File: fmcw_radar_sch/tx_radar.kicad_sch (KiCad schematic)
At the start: 16 parts, among them SW2 SW_Nidec_CAS-120A1, U4 ADAR2001ACCZ

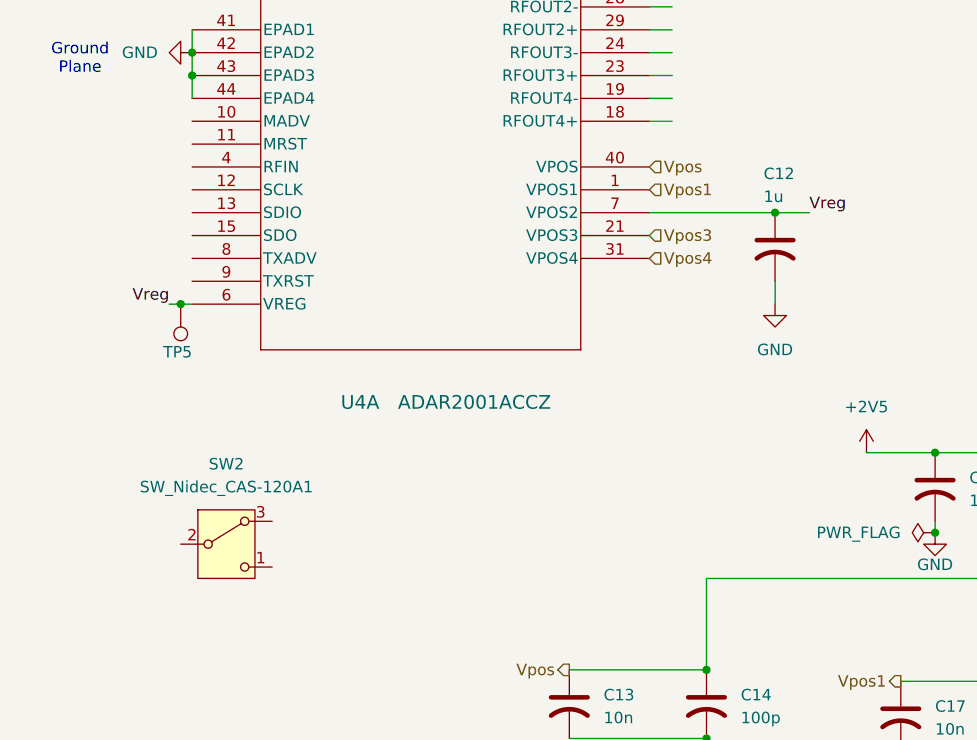
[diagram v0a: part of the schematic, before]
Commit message: Layout of controller board
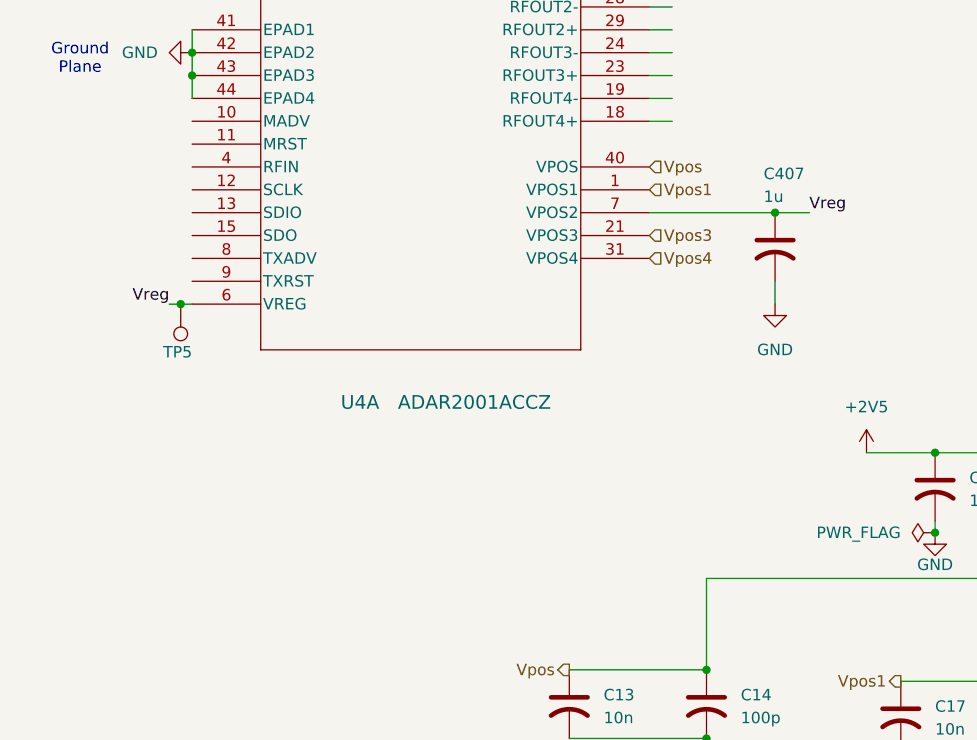
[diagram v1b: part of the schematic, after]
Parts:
- removed C12: 1u, symbol Device:C_US
- removed SW2: SW_Nidec_CAS-120A1, Button_Switch_SMD:Nidec_Copal_CAS-120A, symbol Switch:SW_Nidec_CAS-120A1
- added C407: 1u, symbol Device:C_US
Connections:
- net GND: now also C407.2
- net Vreg: now also C407.1
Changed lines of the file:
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@@
+	)
+	(junction
+		(at 101.6 82.55)
+		(diameter 0)
+		(color 0 0 0 0)
 	)
 	(junction
@@
 	)
 	(junction
-		(at 101.6 82.55)
-		(diameter 0)
-		(color 0 0 0 0)
-	)
-	(junction
 		(at 138.43 123.19)
 		(diameter 0)
@@
 	(wire
 		(pts
+			(xy 101.6 82.55) (xy 105.41 82.55)
+		)
+		(stroke
+			(width 0)
+			(type default)
+		)
+	)
+	(wire
+		(pts
 			(xy 87.63 57.15) (xy 90.17 57.15)
 		)
@@
 	(wire
 		(pts
-			(xy 101.6 82.55) (xy 105.41 82.55)
+			(xy 87.63 82.55) (xy 101.6 82.55)
 		)
 		(stroke
@@
 		(pts
 			(xy 199.39 123.19) (xy 199.39 134.62)
-		)
-		(stroke
-			(width 0)
-			(type default)
-		)
-	)
-	(wire
-		(pts
-			(xy 87.63 82.55) (xy 101.6 82.55)
 		)
 		(stroke
@@
 	)
 	(symbol
-		(lib_id "Switch:SW_Nidec_CAS-120A1")
-		(at 40.64 119.38 0)
-		(unit 1)
-		(exclude_from_sim no)
-		(in_bom yes)
-		(on_board yes)
-		(dnp no)
-		(fields_autoplaced yes)
-		(property "Reference" "SW2"
-			(at 40.64 110.49 0)
-			(effects
-				(font
-					(size 1.27 1.27)
-				)
-			)
-		)
-		(property "Value" "SW_Nidec_CAS-120A1"
-			(at 40.64 113.03 0)
-			(effects
-				(font
-					(size 1.27 1.27)
-				)
-			)
-		)
-		(property "Footprint" "Button_Switch_SMD:Nidec_Copal_CAS-120A"
-			(at 40.64 129.54 0)
-			(effects
-				(font
-					(size 1.27 1.27)
-				)
-				(hide yes)
-			)
-		)
-		(property "Datasheet" "https://www.nidec-components.com/e/catalog/switch/cas.pdf"
-			(at 40.64 127 0)
-			(effects
-				(font
-					(size 1.27 1.27)
-				)
-				(hide yes)
-			)
-		)
-		(property "Description" "Switch, single pole double throw"
-			(at 40.64 119.38 0)
-			(effects
-				(font
-					(size 1.27 1.27)
-				)
-				(hide yes)
-			)
-		)
-		(pin "2"
-		)
-		(pin "3"
-		)
-		(pin "1"
-		)
-		(instances
-			(project ""
-				(path "/435eb955-ea36-4ca2-96a0-71f0d07942fb/622165ea-e76d-4910-b64a-29860b9db6ac"
-					(reference "SW2")
-					(unit 1)
-				)
-			)
-		)
-	)
-	(symbol
 		(lib_id "Device:C_US")
 		(at 78.74 137.16 0)
@@
 	)
 	(symbol
-		(lib_id "Device:C_US")
-		(at 101.6 86.36 0)
-		(unit 1)
-		(exclude_from_sim no)
-		(in_bom yes)
-		(on_board yes)
-		(dnp no)
-		(property "Reference" "C12"
-			(at 100.33 78.232 0)
-			(effects
-				(font
-					(size 1.27 1.27)
-				)
-				(justify left)
-			)
-		)
-		(property "Value" "1u"
-			(at 100.33 80.772 0)
-			(effects
-				(font
-					(size 1.27 1.27)
-				)
-				(justify left)
-			)
-		)
-		(property "Footprint" ""
-			(at 101.6 86.36 0)
-			(effects
-				(font
-					(size 1.27 1.27)
-				)
-				(hide yes)
-			)
-		)
-		(property "Datasheet" ""
-			(at 101.6 86.36 0)
-			(effects
-				(font
-					(size 1.27 1.27)
-				)
-				(hide yes)
-			)
-		)
-		(property "Description" "capacitor, US symbol"
-			(at 101.6 86.36 0)
-			(effects
-				(font
-					(size 1.27 1.27)
-				)
-				(hide yes)
-			)
-		)
-		(pin "1"
-		)
-		(pin "2"
-		)
-		(instances
-			(project "fmcw_radar_sch"
-				(path "/435eb955-ea36-4ca2-96a0-71f0d07942fb/622165ea-e76d-4910-b64a-29860b9db6ac"
-					(reference "C12")
-					(unit 1)
-				)
-			)
-		)
-	)
-	(symbol
 		(lib_id "power:GND")
 		(at 101.6 92.71 0)
@@
 					(unit 1)
 				)
+			)
+		)
+	)
+	(symbol
+		(lib_id "Device:C_US")
+		(at 101.6 86.36 0)
+		(unit 1)
+		(exclude_from_sim no)
+		(in_bom yes)
+		(on_board yes)
+		(dnp no)
+		(property "Reference" "C407"
+			(at 100.33 78.232 0)
+			(effects
+				(font
+					(size 1.27 1.27)
+				)
+				(justify left)
+			)
+		)
+		(property "Value" "1u"
+			(at 100.33 80.772 0)
+			(effects
+				(font
+					(size 1.27 1.27)
+				)
+				(justify left)
+			)
+		)
+		(property "Footprint" ""
+			(at 101.6 86.36 0)
+			(effects
+				(font
+					(size 1.27 1.27)
+				)
+				(hide yes)
+			)
+		)
+		(property "Datasheet" ""
+			(at 101.6 86.36 0)
+			(effects
+				(font
+					(size 1.27 1.27)
+				)
+				(hide yes)
+			)
+		)
+		(property "Description" "capacitor, US symbol"
+			(at 101.6 86.36 0)
+			(effects
+				(font
+					(size 1.27 1.27)
+				)
+				(hide yes)
+			)
+		)
+		(pin "1"
+		)
+		(pin "2"
+		)
+		(instances
+			(project "fmcw_radar_sch"
+				(path "/435eb955-ea36-4ca2-96a0-71f0d07942fb/622165ea-e76d-4910-b64a-29860b9db6ac"
+					(reference "C407")
+					(unit 1)
+				)

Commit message: CHANGES
changes
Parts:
- renumbered C13 to C25, C14 to C26, C407 to C27, C17 to C28, C12 to C29, C18 to C30, C19 to C31, C20 to C32, C21 to C33, C22 to C34, R3 to R18, TP3 to TP1, TP5 to TP2, TP4 to TP3, U4 to U7
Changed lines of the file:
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@@
 		(dnp no)
 		(fields_autoplaced yes)
-		(property "Reference" "R3"
+		(property "Reference" "R18"
 			(at 26.67 46.9899 0)
 			(effects
@@
 			(project "fmcw_radar_sch"
 				(path "/435eb955-ea36-4ca2-96a0-71f0d07942fb/622165ea-e76d-4910-b64a-29860b9db6ac"
-					(reference "R3")
+					(reference "R18")
 					(unit 1)
 				)
@@
 		(dnp no)
 		(fields_autoplaced yes)
-		(property "Reference" "C17"
+		(property "Reference" "C28"
 			(at 119.38 137.4139 0)
 			(effects
@@
 			(project "fmcw_radar_sch"
 				(path "/435eb955-ea36-4ca2-96a0-71f0d07942fb/622165ea-e76d-4910-b64a-29860b9db6ac"
-					(reference "C17")
+					(reference "C28")
 					(unit 1)
 				)
@@
 		(dnp no)
 		(fields_autoplaced yes)
-		(property "Reference" "#PWR030"
+		(property "Reference" "#PWR065"
 			(at 163.83 153.67 0)
 			(effects
@@
 			(project "fmcw_radar_sch"
 				(path "/435eb955-ea36-4ca2-96a0-71f0d07942fb/622165ea-e76d-4910-b64a-29860b9db6ac"
-					(reference "#PWR030")
+					(reference "#PWR065")
 					(unit 1)
 				)
@@
 		(dnp no)
 		(fields_autoplaced yes)
-		(property "Reference" "#PWR024"
+		(property "Reference" "#PWR059"
 			(at 30.48 64.77 0)
 			(effects
@@
 			(project "fmcw_radar_sch"
 				(path "/435eb955-ea36-4ca2-96a0-71f0d07942fb/622165ea-e76d-4910-b64a-29860b9db6ac"
-					(reference "#PWR024")
+					(reference "#PWR059")
 					(unit 1)
 				)
@@
 		(dnp no)
 		(fields_autoplaced yes)
-		(property "Reference" "C12"
+		(property "Reference" "C29"
 			(at 123.19 112.0139 0)
 			(effects
@@
 			(project "fmcw_radar_sch"
 				(path "/435eb955-ea36-4ca2-96a0-71f0d07942fb/622165ea-e76d-4910-b64a-29860b9db6ac"
-					(reference "C12")
+					(reference "C29")
 					(unit 1)
 				)
@@
 		(dnp no)
 		(fields_autoplaced yes)
-		(property "Reference" "C14"
+		(property "Reference" "C26"
 			(at 97.79 136.1439 0)
 			(effects
@@
 			(project "fmcw_radar_sch"
 				(path "/435eb955-ea36-4ca2-96a0-71f0d07942fb/622165ea-e76d-4910-b64a-29860b9db6ac"
-					(reference "C14")
+					(reference "C26")
 					(unit 1)
 				)
@@
 		(dnp no)
 		(fields_autoplaced yes)
-		(property "Reference" "#FLG04"
+		(property "Reference" "#FLG07"
 			(at 26.035 53.34 0)
 			(effects
@@
 			(project "fmcw_radar_sch"
 				(path "/435eb955-ea36-4ca2-96a0-71f0d07942fb/622165ea-e76d-4910-b64a-29860b9db6ac"
-					(reference "#FLG04")
+					(reference "#FLG07")
 					(unit 1)
 				)
@@
 		(dnp no)
 		(fields_autoplaced yes)
-		(property "Reference" "#PWR029"
+		(property "Reference" "#PWR064"
 			(at 130.81 153.67 0)
 			(effects
@@
 			(project "fmcw_radar_sch"
 				(path "/435eb955-ea36-4ca2-96a0-71f0d07942fb/622165ea-e76d-4910-b64a-29860b9db6ac"
-					(reference "#PWR029")
+					(reference "#PWR064")
 					(unit 1)
 				)
@@
 		(dnp no)
 		(fields_autoplaced yes)
-		(property "Reference" "C21"
+		(property "Reference" "C33"
 			(at 187.96 137.4139 0)
 			(effects
@@
 			(project "fmcw_radar_sch"
 				(path "/435eb955-ea36-4ca2-96a0-71f0d07942fb/622165ea-e76d-4910-b64a-29860b9db6ac"
-					(reference "C21")
+					(reference "C33")
 					(unit 1)
 				)
@@
 		(dnp no)
 		(fields_autoplaced yes)
-		(property "Reference" "C13"
+		(property "Reference" "C25"
 			(at 82.55 136.1439 0)
 			(effects
@@
 			(project "fmcw_radar_sch"
 				(path "/435eb955-ea36-4ca2-96a0-71f0d07942fb/622165ea-e76d-4910-b64a-29860b9db6ac"
-					(reference "C13")
+					(reference "C25")
 					(unit 1)
 				)
@@
 		(dnp no)
 		(fields_autoplaced yes)
-		(property "Reference" "C22"
+		(property "Reference" "C34"
 			(at 203.2 137.4139 0)
 			(effects
@@
 			(project "fmcw_radar_sch"
 				(path "/435eb955-ea36-4ca2-96a0-71f0d07942fb/622165ea-e76d-4910-b64a-29860b9db6ac"
-					(reference "C22")
+					(reference "C34")
 					(unit 1)
 				)
@@
 		(on_board yes)
 		(dnp no)
-		(property "Reference" "TP3"
+		(property "Reference" "TP1"
 			(at 18.796 54.61 0)
 			(effects
@@
 			(project "fmcw_radar_sch"
 				(path "/435eb955-ea36-4ca2-96a0-71f0d07942fb/622165ea-e76d-4910-b64a-29860b9db6ac"
-					(reference "TP3")
+					(reference "TP1")
 					(unit 1)
 				)
@@
 		(dnp no)
 		(fields_autoplaced yes)
-		(property "Reference" "#FLG05"
+		(property "Reference" "#FLG08"
 			(at 117.475 118.11 0)
 			(effects
@@
 			(project "fmcw_radar_sch"
 				(path "/435eb955-ea36-4ca2-96a0-71f0d07942fb/622165ea-e76d-4910-b64a-29860b9db6ac"
-					(reference "#FLG05")
+					(reference "#FLG08")
 					(unit 1)
 				)
@@
 		(dnp no)
 		(fields_autoplaced yes)
-		(property "Reference" "#PWR031"
+		(property "Reference" "#PWR066"
 			(at 199.39 153.67 0)
 			(effects
@@
 			(project "fmcw_radar_sch"
 				(path "/435eb955-ea36-4ca2-96a0-71f0d07942fb/622165ea-e76d-4910-b64a-29860b9db6ac"
-					(reference "#PWR031")
+					(reference "#PWR066")
 					(unit 1)
 				)
@@
 		(dnp no)
 		(fields_autoplaced yes)
-		(property "Reference" "C18"
+		(property "Reference" "C30"
 			(at 134.62 137.4139 0)
 			(effects
@@
 			(project "fmcw_radar_sch"
 				(path "/435eb955-ea36-4ca2-96a0-71f0d07942fb/622165ea-e76d-4910-b64a-29860b9db6ac"
-					(reference "C18")
+					(reference "C30")
 					(unit 1)
 				)
@@
 		(dnp no)
 		(fields_autoplaced yes)
-		(property "Reference" "C20"
+		(property "Reference" "C32"
 			(at 167.64 137.4139 0)
 			(effects
@@
 			(project "fmcw_radar_sch"
 				(path "/435eb955-ea36-4ca2-96a0-71f0d07942fb/622165ea-e76d-4910-b64a-29860b9db6ac"
-					(reference "C20")
+					(reference "C32")
 					(unit 1)
 				)
@@
 		(on_board yes)
 		(dnp no)
-		(property "Reference" "U4"
+		(property "Reference" "U7"
 			(at 53.34 103.632 0)
 			(effects
@@
 			(project "fmcw_radar_sch"
 				(path "/435eb955-ea36-4ca2-96a0-71f0d07942fb/622165ea-e76d-4910-b64a-29860b9db6ac"
-					(reference "U4")
+					(reference "U7")
 					(unit 1)
 				)
@@
 		(on_board yes)
 		(dnp no)
-		(property "Reference" "TP5"
+		(property "Reference" "TP2"
 			(at 36.83 98.044 0)
 			(effects
@@
 			(project "fmcw_radar_sch"
 				(path "/435eb955-ea36-4ca2-96a0-71f0d07942fb/622165ea-e76d-4910-b64a-29860b9db6ac"
-					(reference "TP5")
+					(reference "TP2")
 					(unit 1)
 				)
@@
 		(dnp no)
 		(fields_autoplaced yes)
-		(property "Reference" "#PWR025"
+		(property "Reference" "#PWR061"
 			(at 101.6 99.06 0)
 			(effects
@@
 			(project "fmcw_radar_sch"
 				(path "/435eb955-ea36-4ca2-96a0-71f0d07942fb/622165ea-e76d-4910-b64a-29860b9db6ac"
-					(reference "#PWR025")
+					(reference "#PWR061")
 					(unit 1)
 				)
@@
 		(dnp no)
 		(fields_autoplaced yes)
-		(property "Reference" "#PWR035"
+		(property "Reference" "#PWR062"
 			(at 111.76 113.03 0)
 			(effects
@@
 			(project ""
 				(path "/435eb955-ea36-4ca2-96a0-71f0d07942fb/622165ea-e76d-4910-b64a-29860b9db6ac"
-					(reference "#PWR035")
+					(reference "#PWR062")
 					(unit 1)
 				)
@@
 		(on_board yes)
 		(dnp no)
-		(property "Reference" "C407"
+		(property "Reference" "C27"
 			(at 100.33 78.232 0)
 			(effects
@@
 			(project "fmcw_radar_sch"
 				(path "/435eb955-ea36-4ca2-96a0-71f0d07942fb/622165ea-e76d-4910-b64a-29860b9db6ac"
-					(reference "C407")
+					(reference "C27")
 					(unit 1)
 				)
@@
 		(dnp no)
 		(fields_autoplaced yes)
-		(property "Reference" "C19"
+		(property "Reference" "C31"
 			(at 152.4 137.4139 0)
 			(effects
@@
 			(project "fmcw_radar_sch"
 				(path "/435eb955-ea36-4ca2-96a0-71f0d07942fb/622165ea-e76d-4910-b64a-29860b9db6ac"
-					(reference "C19")
+					(reference "C31")
 					(unit 1)
 				)
@@
 		(on_board yes)
 		(dnp no)
-		(property "Reference" "TP4"
+		(property "Reference" "TP3"
 			(at 143.764 107.95 0)
 			(effects
@@
 			(project "fmcw_radar_sch"
 				(path "/435eb955-ea36-4ca2-96a0-71f0d07942fb/622165ea-e76d-4910-b64a-29860b9db6ac"
-					(reference "TP4")
+					(reference "TP3")
 					(unit 1)
 				)
@@
 		(dnp no)
 		(fields_autoplaced yes)
-		(property "Reference" "#PWR026"
+		(property "Reference" "#PWR060"
 			(at 93.98 152.4 0)
 			(effects
@@
 			(project "fmcw_radar_sch"
 				(path "/435eb955-ea36-4ca2-96a0-71f0d07942fb/622165ea-e76d-4910-b64a-29860b9db6ac"
-					(reference "#PWR026")
+					(reference "#PWR060")
 					(unit 1)
 				)
@@
 		(dnp no)
 		(fields_autoplaced yes)
-		(property "Reference" "#PWR041"
+		(property "Reference" "#PWR058"
 			(at 24.13 45.72 0)
 			(effects
@@
 			(project ""
 				(path "/435eb955-ea36-4ca2-96a0-71f0d07942fb/622165ea-e76d-4910-b64a-29860b9db6ac"
-					(reference "#PWR041")
+					(reference "#PWR058")
 					(unit 1)
 				)
@@
 		(on_board yes)
 		(dnp no)
-		(property "Reference" "#PWR028"
+		(property "Reference" "#PWR063"
 			(at 119.38 124.46 0)
 			(effects
@@
 			(project "fmcw_radar_sch"
 				(path "/435eb955-ea36-4ca2-96a0-71f0d07942fb/622165ea-e76d-4910-b64a-29860b9db6ac"
-					(reference "#PWR028")
-					(unit 1)
-				)
+					(reference "#PWR063")
+					(unit 1)
+				)
